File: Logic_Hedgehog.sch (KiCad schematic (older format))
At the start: 70 parts, among them J40 RaspberryPI3, J41 UART_EXT_1, J42 I2C_EXT_0, J43 I2C_EXT_0_EXP, J44 I2C_EXT_1, J45 SPI_EXT_0_0, J46 SPI_EXT_0_1, J47 SPI_EXT_1, J48 Digital, J49 Analog, J50 Digital, J51 Analog, J52 SERVO, J53 SERVO, J54 MOTORS, J55 MOTORS, U40 STM32F401VBT6, U41 74LVC2G32, U42 MC74VHC1G126, U43 IMU_ICM-20689, U44 DRV8835, U45 DRV8835, U46 Buzzer, Y40 Crystal

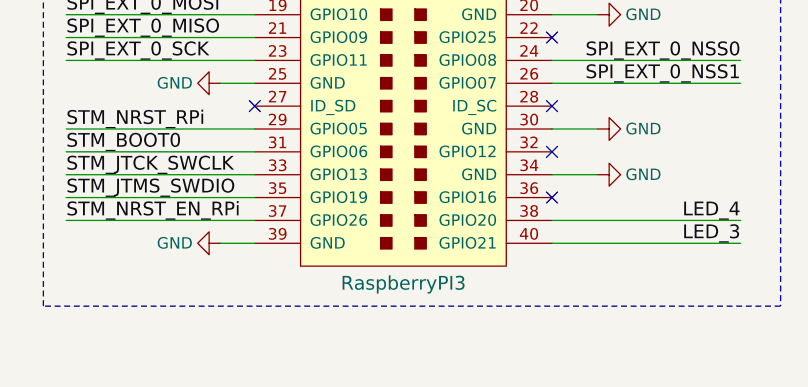
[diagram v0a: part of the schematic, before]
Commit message: changed L and D of RPi 5V reg, all components on one side, everything routed, silkscreen unfinished
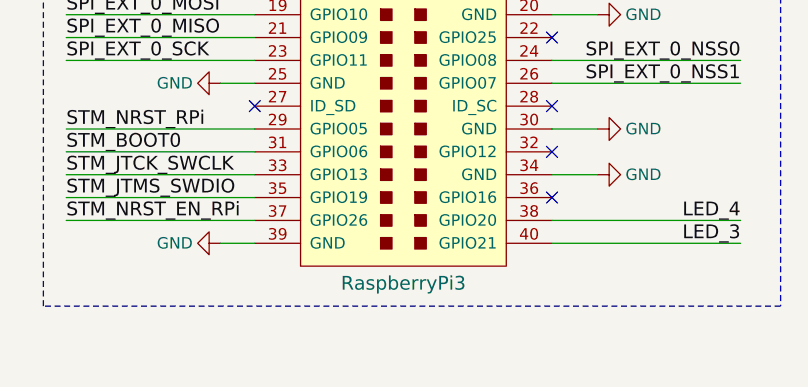
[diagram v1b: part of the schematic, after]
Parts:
- J40: value RaspberryPI3 -> RaspberryPi3
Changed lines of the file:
@@
 P 2750 9400
 F 0 "J40" H 2750 10450 60  0000 C CNN
-F 1 "RaspberryPI3" H 2750 8225 60  0000 C CNN
+F 1 "RaspberryPi3" H 2750 8225 60  0000 C CNN
 F 2 "Socket_Strips:Socket_Strip_Straight_2x20_Pitch2.54mm" H 2750 8375 60  0001 C CNN
 F 3 "" H 2750 8375 60  0001 C CNN

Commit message: probably the final version for the prototypes, gerbers added
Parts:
- removed R44: 0R, Resistors_SMD:R_0603, symbol R
- R40, R41: value R -> 1k8
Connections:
- net at U40.12 (PH0-OSC_IN): now also C46.1, Y40.2
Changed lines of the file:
@@
 P 7350 9900
 F 0 "R41" H 7400 9925 50  0000 L CNN
-F 1 "R" H 7400 9850 50  0000 L CNN
+F 1 "1k8" H 7400 9850 50  0000 L CNN
 F 2 "Resistors_SMD:R_0603" V 7280 9900 50  0001 C CNN
 F 3 "" H 7350 9900 50  0001 C CNN
@@
 P 4000 6525
 F 0 "R40" H 3800 6575 50  0000 L CNN
-F 1 "R" H 3800 6475 50  0000 L CNN
+F 1 "1k8" H 3800 6475 50  0000 L CNN
 F 2 "Resistors_SMD:R_0603" V 3930 6525 50  0001 C CNN
 F 3 "" H 4000 6525 50  0001 C CNN
@@
 F 3 "" H 4525 6400 50  0001 C CNN
 	1    4525 6400
-	1    0    0    -1
-$EndComp
-$Comp
-L R R44
-U 1 1 590FEEE9
-P 4625 6400
-F 0 "R44" H 4650 6625 50  0000 L CNN
-F 1 "0R" H 4650 6550 50  0000 L CNN
-F 2 "Resistors_SMD:R_0603" V 4555 6400 50  0001 C CNN
-F 3 "" H 4625 6400 50  0001 C CNN
-	1    4625 6400
 	1    0    0    -1
 $EndComp
@@
 	4525 6125 4525 6250
 Wire Wire Line
-	4625 6125 4625 6250
+	4625 6125 4625 6900
 Wire Wire Line
 	4275 6575 4275 6900
@@
 Connection ~ 4275 6775
 Wire Wire Line
-	4625 6550 4625 6900
-Wire Wire Line
 	4600 6775 4625 6775

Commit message: just small changes
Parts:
- Y40: footprint Crystals:Crystal_HC49-U_Vertical -> Crystals:Crystal_HC49-4H_Vertical
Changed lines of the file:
@@
 F 0 "Y40" H 4450 6925 50  0000 C CNN
 F 1 "Crystal" H 4450 6625 50  0000 C CNN
-F 2 "Crystals:Crystal_HC49-U_Vertical" H 4450 6775 50  0001 C CNN
+F 2 "Crystals:Crystal_HC49-4H_Vertical" H 4450 6775 50  0001 C CNN
 F 3 "" H 4450 6775 50  0001 C CNN
 	1    4450 6775
@@
 U 1 1 590FD684
 P 5325 4225
+AR Path="/590FD684" Ref="U40"  Part="1"
+AR Path="/58F4F058/590FD684" Ref="U40"  Part="1"
 F 0 "U40" H 6400 6100 60  0000 C CNN
 F 1 "STM32F401VBT6" H 6700 6000 60  0000 C CNN

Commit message: added thermals to gnd and 3v3 tht pads
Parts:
- J40: footprint Socket_Strips:Socket_Strip_Straight_2x20_Pitch2.54mm -> hedgehog_footprints:Socket_Strip_Straight_2x20_Pitch2.54mm_thermals
- J50, J51: footprint Socket_Strips:Socket_Strip_Straight_2x08_Pitch2.54mm -> hedgehog_footprints:Socket_Strip_Straight_2x08_Pitch2.54mm_thermals
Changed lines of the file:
@@
 F 0 "J40" H 2750 10450 60  0000 C CNN
 F 1 "RaspberryPi3" H 2750 8225 60  0000 C CNN
-F 2 "Socket_Strips:Socket_Strip_Straight_2x20_Pitch2.54mm" H 2750 8375 60  0001 C CNN
+F 2 "hedgehog_footprints:Socket_Strip_Straight_2x20_Pitch2.54mm_thermals" H 2750 8375 60  0001 C CNN
 F 3 "" H 2750 8375 60  0001 C CNN
 	1    2750 9400
@@
 F 0 "J50" H 14750 2350 50  0000 C CNN
 F 1 "Digital" V 14750 1900 50  0000 C CNN
-F 2 "Socket_Strips:Socket_Strip_Straight_2x08_Pitch2.54mm" H 14750 700 50  0001 C CNN
+F 2 "hedgehog_footprints:Socket_Strip_Straight_2x08_Pitch2.54mm_thermals" H 14750 700 50  0001 C CNN
 F 3 "" H 14750 700 50  0001 C CNN
 	1    14750 1900
@@
 F 0 "J51" H 14750 4125 50  0000 C CNN
 F 1 "Analog" V 14750 3675 50  0000 C CNN
-F 2 "Socket_Strips:Socket_Strip_Straight_2x08_Pitch2.54mm" H 14750 2475 50  0001 C CNN
+F 2 "hedgehog_footprints:Socket_Strip_Straight_2x08_Pitch2.54mm_thermals" H 14750 2475 50  0001 C CNN
 F 3 "" H 14750 2475 50  0001 C CNN
 	1    14750 3675

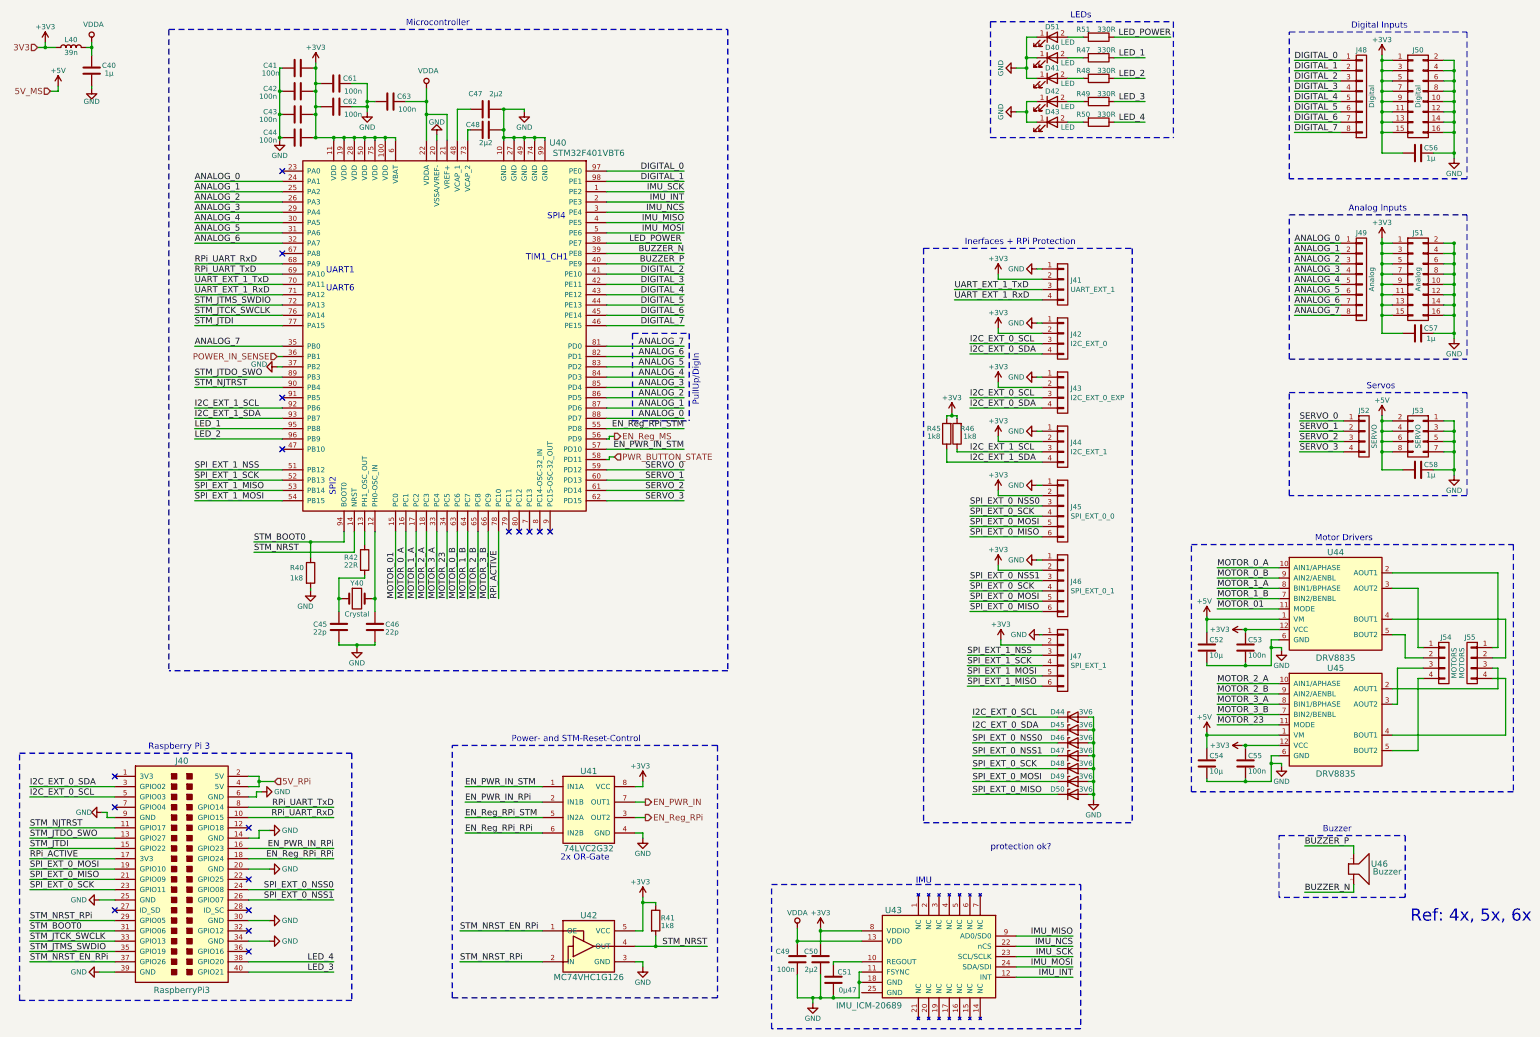
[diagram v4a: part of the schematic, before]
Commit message: lots of changes: - incremented version number to 0.2 - all inputs are now analog, vbat for supply voltage monitoring - 6 servos - different 5v 10A regulator - changed input order - footprint fixes and cosmetic hanges - added fiducials - board size 0.5mm smaller - lots of other fixes and small changes
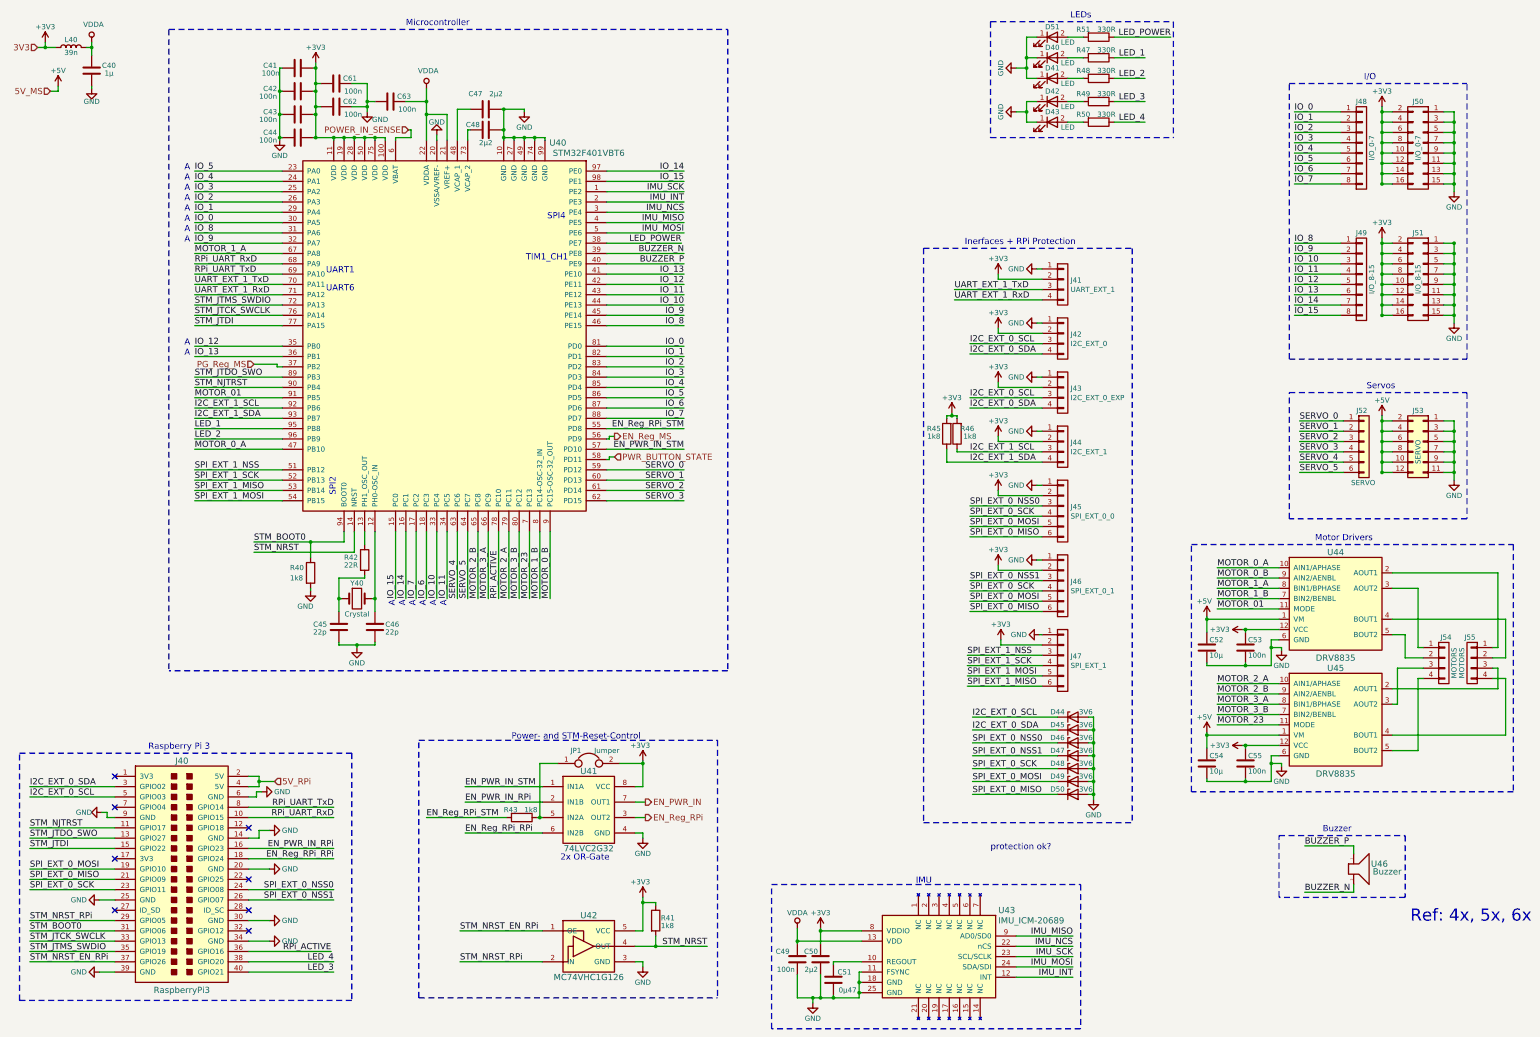
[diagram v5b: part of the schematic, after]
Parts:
- removed C56, C57, C58: 1µ, Capacitors_SMD:C_0603, symbol C
- removed J52: SERVO, Pin_Headers:Pin_Header_Straight_1x04_Pitch2.54mm, symbol CONN_01X04
- removed J53: SERVO, Pin_Headers:Pin_Header_Straight_2x04_Pitch2.54mm, symbol CONN_02X04
- added J52: SERVO, hedgehog_footprints:Pin_Header_Straight_1x06_Pitch2.54mm_servo, symbol Conn_01x06
- added J53: SERVO, hedgehog_footprints:Pin_Header_Straight_2x06_Pitch2.54mm_thermals, symbol Conn_02x06_Odd_Even
- added JP1: Jumper, hedgehog_footprints:Pin_Header_Straight_1x02_Pitch2.54mm, symbol Jumper
- added R43: 1k8, Resistors_SMD:R_0603, symbol R
- J41, J42, J43, J44: footprint Socket_Strips:Socket_Strip_Straight_1x04_Pitch2.54mm -> hedgehog_footprints:Socket_Strip_Straight_1x04_Pitch2.54mm
- J45, J46, J47: footprint Socket_Strips:Socket_Strip_Straight_1x06_Pitch2.54mm -> hedgehog_footprints:Socket_Strip_Straight_1x06_Pitch2.54mm
- J48: value Digital -> I/O_0-7; footprint Socket_Strips:Socket_Strip_Straight_1x08_Pitch2.54mm -> hedgehog_footprints:Socket_Strip_Straight_1x08_Pitch2.54mm
- J49: value Analog -> I/O_8-15; footprint Socket_Strips:Socket_Strip_Straight_1x08_Pitch2.54mm -> hedgehog_footprints:Socket_Strip_Straight_1x08_Pitch2.54mm
- J50: value Digital -> I/O_0-7
- J51: value Analog -> I/O_8-15
- J54, J55: footprint Socket_Strips:Socket_Strip_Straight_1x04_Pitch2.54mm -> hedgehog_footprints:Socket_Strip_Straight_1x04_Pitch2.54mm_motor
- L40: footprint Inductors_SMD:L_0603_HandSoldering -> Inductors_SMD:L_0603
- U43: footprint Housings_DFN_QFN:QFN-24_4x4mm_Pitch0.5mm -> Housings_DFN_QFN:QFN-24-1EP_4x4mm_Pitch0.5mm
- Y40: footprint Crystals:Crystal_HC49-4H_Vertical -> Crystals:Crystal_SMD_HC49-SD
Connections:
- net +3V3: now also J50.10 (P10), J50.12 (P12), J50.14 (P14), J50.16 (P16), J50.2 (P2), J50.4 (P4), J50.6 (P6), J50.8 (P8), J51.10 (P10), J51.12 (P12), J51.14 (P14), J51.16 (P16), J51.2 (P2), J51.4 (P4), J51.6 (P6), J51.8 (P8), JP1.2; no longer J50.1 (P1), J50.11 (P11), J50.13 (P13), J50.15 (P15), J50.3 (P3), J50.5 (P5), J50.7 (P7), J50.9 (P9), J51.1 (P1), J51.11 (P11), J51.13 (P13), J51.15 (P15), J51.3 (P3), J51.5 (P5), J51.7 (P7), J51.9 (P9), U40.6 (VBAT)
- net +5V: now also J53.10 (Pin_10), J53.12 (Pin_12), J53.2 (Pin_2), J53.4 (Pin_4), J53.6 (Pin_6), J53.8 (Pin_8)
- net EN_Reg_RPi_STM: now also R43.2; no longer U41.5 (IN2A)
- net GND: now also J50.1 (P1), J50.11 (P11), J50.13 (P13), J50.15 (P15), J50.3 (P3), J50.5 (P5), J50.7 (P7), J50.9 (P9), J51.1 (P1), J51.11 (P11), J51.13 (P13), J51.15 (P15), J51.3 (P3), J51.5 (P5), J51.7 (P7), J51.9 (P9), U43.25 (GND), J53.1 (Pin_1), J53.11 (Pin_11), J53.3 (Pin_3), J53.5 (Pin_5), J53.7 (Pin_7), J53.9 (Pin_9); no longer J50.10 (P10), J50.12 (P12), J50.14 (P14), J50.16 (P16), J50.2 (P2), J50.4 (P4), J50.6 (P6), J50.8 (P8), J51.10 (P10), J51.12 (P12), J51.14 (P14), J51.16 (P16), J51.2 (P2), J51.4 (P4), J51.6 (P6), J51.8 (P8), U40.37 (PB2)
- net MOTOR_01: now also U40.91 (PB5); no longer U40.15 (PC0)
- net MOTOR_0_A: now also U40.47 (PB10); no longer U40.16 (PC1)
- net MOTOR_0_B: now also U40.9 (PC15-OSC-32_OUT); no longer U40.63 (PC6)
- net MOTOR_1_A: now also U40.67 (PA8); no longer U40.17 (PC2)
- net MOTOR_1_B: now also U40.8 (PC14-OSC-32_IN); no longer U40.64 (PC7)
- net MOTOR_23: now also U40.7 (PC13); no longer U40.34 (PC5)
- net MOTOR_2_A: now also U40.79 (PC11); no longer U40.18 (PC3)
- net MOTOR_3_A: now also U40.66 (PC9); no longer U40.33 (PC4)
- net MOTOR_3_B: now also U40.80 (PC12); no longer U40.66 (PC9)
- net POWER_IN_SENSE: now also U40.6 (VBAT); no longer U40.36 (PB1)
- net RPi_ACTIVE: now also J40.36 (GPIO16); no longer J40.17 (3V3)
- net SERVO_0: now also J52.1 (Pin_1)
- net SERVO_1: now also J52.2 (Pin_2)
- net SERVO_2: now also J52.3 (Pin_3)
- net SERVO_3: now also J52.4 (Pin_4)
- net IO_5: now reaches U40.23 (PA0)
- net IO_5: now also J48.6 (P6), U40.86 (PD5)
- removed net ANALOG_0: J49.1 (P1), U40.24 (PA1), U40.88 (PD7)
- removed net ANALOG_1: J49.2 (P2), U40.25 (PA2), U40.87 (PD6)
- removed net ANALOG_2: J49.3 (P3), U40.26 (PA3), U40.86 (PD5)
- removed net ANALOG_3: J49.4 (P4), U40.29 (PA4), U40.85 (PD4)
- removed net ANALOG_4: J49.5 (P5), U40.30 (PA5), U40.84 (PD3)
- removed net ANALOG_5: J49.6 (P6), U40.31 (PA6), U40.83 (PD2)
- removed net ANALOG_6: J49.7 (P7), U40.32 (PA7), U40.82 (PD1)
- removed net ANALOG_7: J49.8 (P8), U40.35 (PB0), U40.81 (PD0)
- net DIGITAL_0 renamed IO_0
- net IO_0: now also U40.30 (PA5), U40.81 (PD0); no longer U40.97 (PE0)
- net DIGITAL_1 renamed IO_1
- net IO_1: now also U40.29 (PA4), U40.82 (PD1); no longer U40.98 (PE1)
- net DIGITAL_2 renamed IO_13
- net IO_13: now also J49.6 (P6), U40.36 (PB1); no longer J48.3 (P3)
- net DIGITAL_3 renamed IO_12
- net IO_12: now also J49.5 (P5), U40.35 (PB0); no longer J48.4 (P4)
- net DIGITAL_4 renamed IO_11
- net IO_11: now also J49.4 (P4), U40.34 (PC5); no longer J48.5 (P5)
- net DIGITAL_5 renamed IO_10
- net IO_10: now also J49.3 (P3), U40.33 (PC4); no longer J48.6 (P6)
- net DIGITAL_6 renamed IO_6
- net IO_6: now also U40.18 (PC3), U40.87 (PD6); no longer U40.45 (PE14)
- net DIGITAL_7 renamed IO_7
- net IO_7: now also U40.17 (PC2), U40.88 (PD7); no longer U40.46 (PE15)
- new net: JP1.1, R43.1, U41.5 (IN2A)
- new net IO_14: J49.7 (P7), U40.16 (PC1), U40.97 (PE0)
- new net IO_15: J49.8 (P8), U40.15 (PC0), U40.98 (PE1)
- new net IO_2: J48.3 (P3), U40.26 (PA3), U40.83 (PD2)
- new net IO_3: J48.4 (P4), U40.25 (PA2), U40.84 (PD3)
- new net IO_4: J48.5 (P5), U40.24 (PA1), U40.85 (PD4)
- new net IO_8: J49.1 (P1), U40.31 (PA6), U40.46 (PE15)
- new net IO_9: J49.2 (P2), U40.32 (PA7), U40.45 (PE14)
- new net PG_Reg_MS: U40.37 (PB2)
- new net SERVO_4: J52.5 (Pin_5), U40.63 (PC6)
- new net SERVO_5: J52.6 (Pin_6), U40.64 (PC7)
- no-connect marks 17 -> 8
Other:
- note added: "A"
- note added: "I/O"
- note removed: "Analog Inputs"
- note removed: "Digital Inputs"
- note removed: "PullUp/DigIn"
- moved on the sheet: J48, J50

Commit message: small changes
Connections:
- net BUZZER_N renamed SPEAKER_N
- net BUZZER_P renamed SPEAKER_P
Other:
- note added: "Speaker"
- note removed: "Buzzer"
- note removed: "protection ok?"
